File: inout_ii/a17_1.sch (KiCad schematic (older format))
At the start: 54 parts, among them U17001 74HC02, U17002 74HC04, U17004 74LVC07, U17005 74HC02, U17006 74HC02, U17007 74HC27, U17008 74HC02, U17009 74HC27, U17010 74HC02, U17011 74HC02, U17012 74HC27, U17013 74LVC07, U17014 74HC02, U17015 74HC02, U17016 74HC27, U17017 74HC02, U17018 74HC02, U17019 74HC27, U17020 74LVC07, U17021 74HC02, U17022 74HC02, U17023 74HC27, U17024 74HC02, U17025 74HC27, U17026 74HC02, U17027 74HC27, U17028 74LVC07, U17029 74HC27, U17030 74HC02, U17031 74HC02, U17032 74HC02, U17033 74HC4002, U17034 74HC27, U17035 74HC02, U17036 74HC27, U17037 74HC02

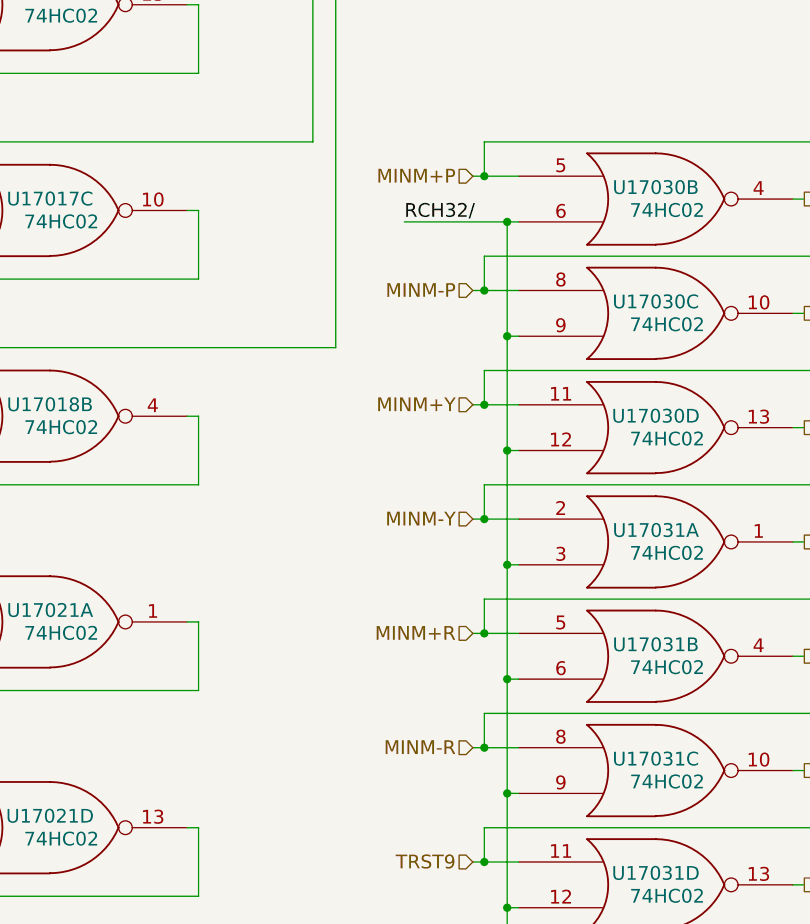
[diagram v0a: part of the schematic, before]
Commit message: Tied in Inout II.
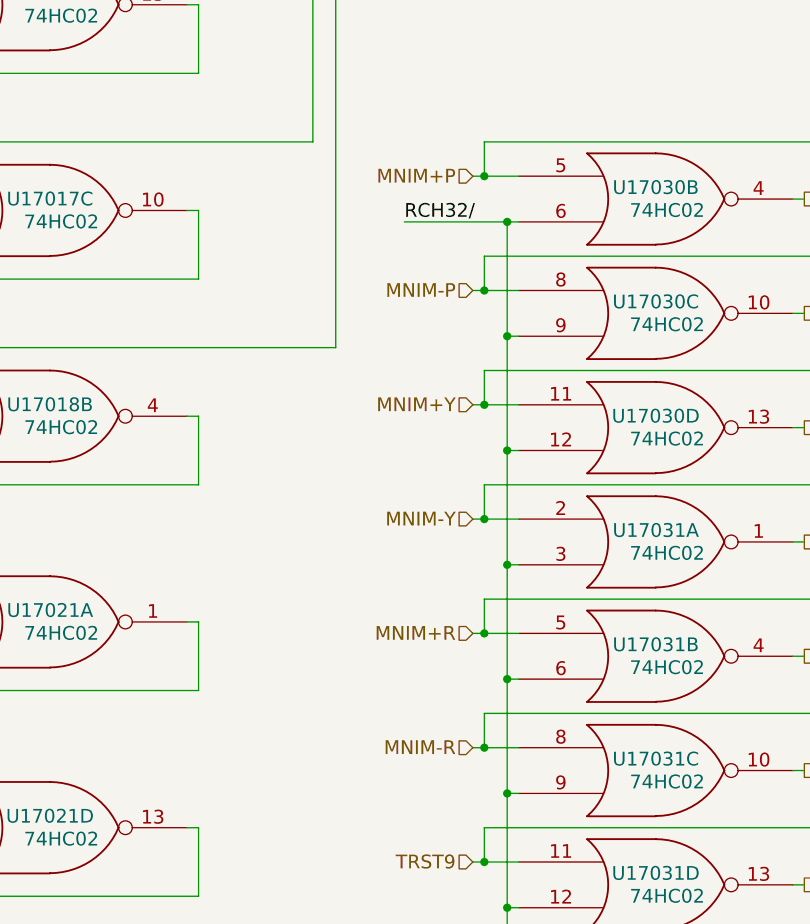
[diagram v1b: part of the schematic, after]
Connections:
- net MINM+P renamed MNIM+P
- net MINM+R renamed MNIM+R
- net MINM+Y renamed MNIM+Y
- net MINM-P renamed MNIM-P
- net MINM-R renamed MNIM-R
- net MINM-Y renamed MNIM-Y
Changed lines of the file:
@@
 $EndComp
 $Comp
-L VCC #PWR08
+L VCC #PWR05
 U 1 1 570994C4
 P 8600 1950
-F 0 "#PWR08" H 8600 1800 50  0001 C CNN
+F 0 "#PWR05" H 8600 1800 50  0001 C CNN
 F 1 "VCC" H 8600 2100 50  0000 C CNN
 F 2 "" H 8600 1950 60  0000 C CNN
@@
 $EndComp
 $Comp
-L VCC #PWR09
+L VCC #PWR06
 U 1 1 570A6C03
 P 8600 2850
-F 0 "#PWR09" H 8600 2700 50  0001 C CNN
+F 0 "#PWR06" H 8600 2700 50  0001 C CNN
 F 1 "VCC" H 8600 3000 50  0000 C CNN
 F 2 "" H 8600 2850 60  0000 C CNN
@@
 $EndComp
 $Comp
-L VCC #PWR010
+L VCC #PWR07
 U 1 1 570B4745
 P 8600 3750
-F 0 "#PWR010" H 8600 3600 50  0001 C CNN
+F 0 "#PWR07" H 8600 3600 50  0001 C CNN
 F 1 "VCC" H 8600 3900 50  0000 C CNN
 F 2 "" H 8600 3750 60  0000 C CNN
@@
 $EndComp
 $Comp
-L VCC #PWR011
+L VCC #PWR08
 U 1 1 570BCCBC
 P 8600 4650
-F 0 "#PWR011" H 8600 4500 50  0001 C CNN
+F 0 "#PWR08" H 8600 4500 50  0001 C CNN
 F 1 "VCC" H 8600 4800 50  0000 C CNN
 F 2 "" H 8600 4650 60  0000 C CNN
@@
 $EndComp
 $Comp
-L VCC #PWR012
+L VCC #PWR09
 U 1 1 570CA6A0
 P 8600 5550
-F 0 "#PWR012" H 8600 5400 50  0001 C CNN
+F 0 "#PWR09" H 8600 5400 50  0001 C CNN
 F 1 "VCC" H 8600 5700 50  0000 C CNN
 F 2 "" H 8600 5550 60  0000 C CNN
@@
 $EndComp
 $Comp
-L VCC #PWR013
+L VCC #PWR010
 U 1 1 570DE648
 P 8600 6450
-F 0 "#PWR013" H 8600 6300 50  0001 C CNN
+F 0 "#PWR010" H 8600 6300 50  0001 C CNN
 F 1 "VCC" H 8600 6600 50  0000 C CNN
 F 2 "" H 8600 6450 60  0000 C CNN
@@
 $EndComp
 $Comp
-L VCC #PWR014
+L VCC #PWR011
 U 1 1 570EE03D
 P 8600 7350
-F 0 "#PWR014" H 8600 7200 50  0001 C CNN
+F 0 "#PWR011" H 8600 7200 50  0001 C CNN
 F 1 "VCC" H 8600 7500 50  0000 C CNN
 F 2 "" H 8600 7350 60  0000 C CNN
@@
 $EndComp
 $Comp
-L VCC #PWR015
+L VCC #PWR012
 U 1 1 570FC497
 P 8600 8250
-F 0 "#PWR015" H 8600 8100 50  0001 C CNN
+F 0 "#PWR012" H 8600 8100 50  0001 C CNN
 F 1 "VCC" H 8600 8400 50  0000 C CNN
 F 2 "" H 8600 8250 60  0000 C CNN
@@
 $EndComp
 $Comp
-L VCC #PWR016
+L VCC #PWR013
 U 1 1 5711F90C
 P 8600 9150
-F 0 "#PWR016" H 8600 9000 50  0001 C CNN
+F 0 "#PWR013" H 8600 9000 50  0001 C CNN
 F 1 "VCC" H 8600 9300 50  0000 C CNN
 F 2 "" H 8600 9150 60  0000 C CNN
@@
 $EndComp
 $Comp
-L VCC #PWR017
+L VCC #PWR014
 U 1 1 5713DFD1
 P 8600 10050
-F 0 "#PWR017" H 8600 9900 50  0001 C CNN
+F 0 "#PWR014" H 8600 9900 50  0001 C CNN
 F 1 "VCC" H 8600 10200 50  0000 C CNN
 F 2 "" H 8600 10050 60  0000 C CNN
@@
 $EndComp
 $Comp
-L VCC #PWR018
+L VCC #PWR015
 U 1 1 571616FE
 P 8600 10950
-F 0 "#PWR018" H 8600 10800 50  0001 C CNN
+F 0 "#PWR015" H 8600 10800 50  0001 C CNN
 F 1 "VCC" H 8600 11100 50  0000 C CNN
 F 2 "" H 8600 10950 60  0000 C CNN
@@
 $EndComp
 $Comp
-L VCC #PWR019
+L VCC #PWR016
 U 1 1 571812F9
 P 8600 11850
-F 0 "#PWR019" H 8600 11700 50  0001 C CNN
+F 0 "#PWR016" H 8600 11700 50  0001 C CNN
 F 1 "VCC" H 8600 12000 50  0000 C CNN
 F 2 "" H 8600 11850 60  0000 C CNN
@@
 $EndComp
 $Comp
-L VCC #PWR020
+L VCC #PWR017
 U 1 1 571A7A2A
 P 8600 12750
-F 0 "#PWR020" H 8600 12600 50  0001 C CNN
+F 0 "#PWR017" H 8600 12600 50  0001 C CNN
 F 1 "VCC" H 8600 12900 50  0000 C CNN
 F 2 "" H 8600 12750 60  0000 C CNN
@@
 $EndComp
 $Comp
-L VCC #PWR021
+L VCC #PWR018
 U 1 1 571CD8B8
 P 8600 13650
-F 0 "#PWR021" H 8600 13500 50  0001 C CNN
+F 0 "#PWR018" H 8600 13500 50  0001 C CNN
 F 1 "VCC" H 8600 13800 50  0000 C CNN
 F 2 "" H 8600 13650 60  0000 C CNN
@@
 $EndComp
 $Comp
-L VCC #PWR022
+L VCC #PWR019
 U 1 1 571ED231
 P 8600 14550
-F 0 "#PWR022" H 8600 14400 50  0001 C CNN
+F 0 "#PWR019" H 8600 14400 50  0001 C CNN
 F 1 "VCC" H 8600 14700 50  0000 C CNN
 F 2 "" H 8600 14550 60  0000 C CNN
@@
 $EndComp
 $Comp
-L VCC #PWR023
+L VCC #PWR020
 U 1 1 5723C90F
 P 14100 4050
-F 0 "#PWR023" H 14100 3900 50  0001 C CNN
+F 0 "#PWR020" H 14100 3900 50  0001 C CNN
 F 1 "VCC" H 14100 4200 50  0000 C CNN
 F 2 "" H 14100 4050 60  0000 C CNN
@@
 $EndComp
 $Comp
-L VCC #PWR024
+L VCC #PWR021
 U 1 1 572CF365
 P 14100 7200
-F 0 "#PWR024" H 14100 7050 50  0001 C CNN
+F 0 "#PWR021" H 14100 7050 50  0001 C CNN
 F 1 "VCC" H 14100 7350 50  0000 C CNN
 F 2 "" H 14100 7200 60  0000 C CNN
@@
 	12550 11150 12750 11150
 Text HLabel 12550 11150 0    60   Input ~ 0
-MINM+P
+MNIM+P
 Wire Wire Line
 	12250 11350 12750 11350
@@
 	12550 11650 12750 11650
 Text HLabel 12550 11650 0    60   Input ~ 0
-MINM-P
+MNIM-P
 Wire Wire Line
 	12700 11350 12700 15850
@@
 	12550 12150 12750 12150
 Text HLabel 12550 12150 0    60   Input ~ 0
-MINM+Y
+MNIM+Y
 Wire Wire Line
 	12700 12350 12750 12350
@@
 	12550 12650 12750 12650
 Text HLabel 12550 12650 0    60   Input ~ 0
-MINM-Y
+MNIM-Y
 Wire Wire Line
 	12700 12850 12750 12850
@@
 	12550 13150 12750 13150
 Text HLabel 12550 13150 0    60   Input ~ 0
-MINM+R
+MNIM+R
 Wire Wire Line
 	12700 13350 12750 13350
@@
 	12550 13650 12750 13650
 Text HLabel 12550 13650 0    60   Input ~ 0
-MINM-R
+MNIM-R
 Wire Wire Line
 	12700 13850 12750 13850
@@
 $EndComp
 $Comp
-L VCC #PWR025
+L VCC #PWR022
 U 1 1 5738D6B5
 P 17050 12350
-F 0 "#PWR025" H 17050 12200 50  0001 C CNN
+F 0 "#PWR022" H 17050 12200 50  0001 C CNN
 F 1 "VCC" H 17050 12500 50  0000 C CNN
 F 2 "" H 17050 12350 60  0000 C CNN

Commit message: Fixed not->1-input nor in the rest of the modules.
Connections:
- net F04B: no longer U17002.11
- net F04B/: no longer U17002.10
- net RCH30/: no longer U17002.4
- net RCH31/: no longer U17002.6
- net RCH32/: no longer U17002.8
- net RCH33/: no longer U17002.2
- net at U17001.4: no longer U17002.1
- net at U17001.13: no longer U17002.3
- net at U17005.4: no longer U17002.5
- net at U17022.13: no longer U17002.9
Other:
- moved on the sheet: U17001B, U17001D, U17002A, U17002B, U17002C, U17002D, U17002E, U17005B, U17022D

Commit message: Updated Inout II to be on +4VSW
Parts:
- renumbered U17004 to U17003, U17005 to U17004, U17006 to U17005, U17007 to U17006, U17008 to U17007, U17009 to U17008, U17010 to U17009, U17011 to U17010, U17012 to U17011, U17013 to U17012, U17014 to U17013, U17015 to U17014, U17016 to U17015, U17017 to U17016, U17018 to U17017, U17019 to U17018, U17020 to U17019, U17021 to U17020, U17022 to U17021, U17023 to U17022, U17024 to U17023, U17025 to U17024, U17026 to U17025, U17027 to U17026, U17028 to U17027, U17029 to U17028, U17030 to U17029, U17031 to U17030, U17032 to U17031, U17033 to U17032, U17034 to U17033, U17035 to U17034, U17036 to U17035, U17037 to U17036
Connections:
- net labels added: +4VSW
- net labels removed: VCC
